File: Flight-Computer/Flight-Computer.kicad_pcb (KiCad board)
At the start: 4 copper layers, 93.7 x 43.7 mm, 120 parts, among them J1 Jumper_NO, J2 Jumper_NO, P1 647676-2, P10 Micro_SD_Card, P2 1546551-2, P3 3220-20-0200-00, P4 440054-3, P5 440054-3, P6 440054-3, P7 440054-3, P8 USB, P9 1984659, Q1 QS5U17TR, Q2 QS5U17TR, Q3 QS5U17TR, Q4 QS5U17TR, Q5 QS5U17TR, Q6 QS5U17TR, U1 STM32H750VBTx, U10 TS391IYLT, U11 TS391IYLT, U12 BMM350, U13 S-85S1AB33-I6T1U, U2 LMS8117AMP-3.3_NOPB, U3 BMI323, U4 MAX-8C-0-10, U5 BMP390, U6 SST25VF040B-50-4I-S2AE-T, U7 RFM95W-868S2, U8 CP2102-GMR(QFN28), U9 TS391IYLT, Y1 ECS-240-18-33-JGN-TR

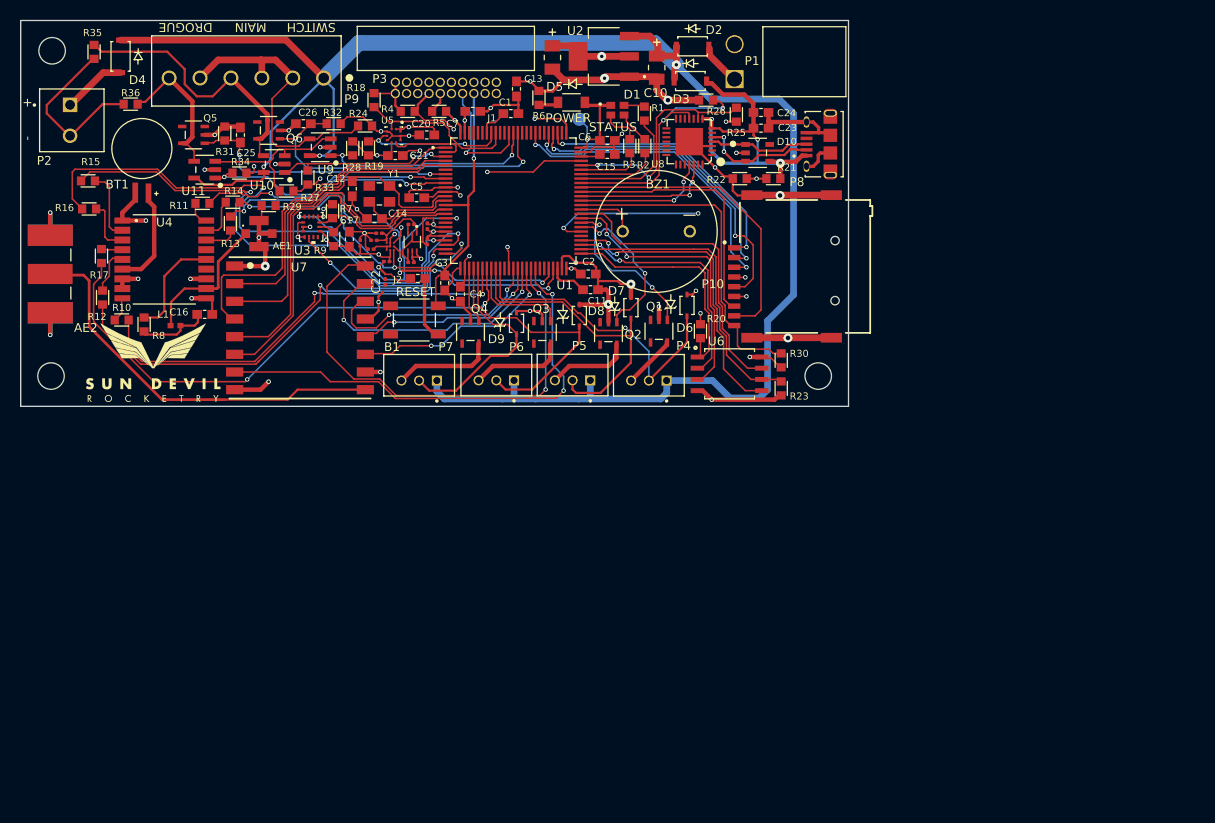
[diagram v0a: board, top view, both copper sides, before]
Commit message: LDO update
Changed buck 1.8V converter to LDO
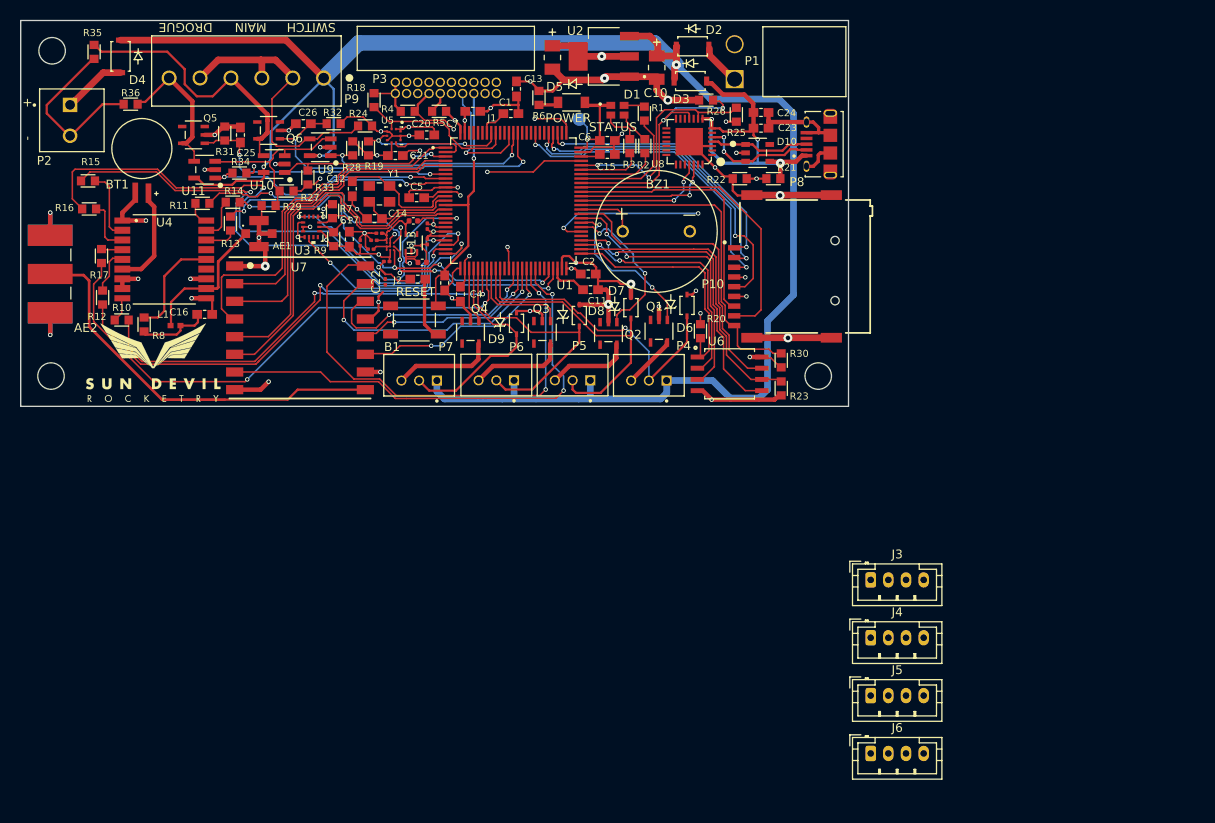
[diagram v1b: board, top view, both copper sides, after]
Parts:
- removed L2: 2.2uH, Inductor_SMD:L_0201_0603Metric
- added C30: 1uF, Capacitor_SMD:C_0402_1005Metric, F.Cu at (137.4, 80.6)
- added J3: Conn_01x04, Connector_JST:JST_PH_B4B-PH-K_1x04_P2.00mm_Vertical, F.Cu at (189.2, 121.2)
- added J4: Conn_01x04, Connector_JST:JST_PH_B4B-PH-K_1x04_P2.00mm_Vertical, F.Cu at (189.2, 127.8)
- added J5: Conn_01x04, Connector_JST:JST_PH_B4B-PH-K_1x04_P2.00mm_Vertical, F.Cu at (189.2, 134.3)
- added J6: Conn_01x04, Connector_JST:JST_PH_B4B-PH-K_1x04_P2.00mm_Vertical, F.Cu at (189.2, 140.9)
- C29: value 10uF -> 1uF; footprint Capacitor_SMD:C_0201_0603Metric -> Capacitor_SMD:C_0402_1005Metric
- U13: value S-85S1AB33-I6T1U -> MIC5365-1.8YC5-TR; footprint S85S1A:SNT-6A-A-PKG_PG006-A-P-SD-2.1_ABL -> MIC5365:SC-70_C5_MCH-L
- moved C29 1.26 mm to (138.4, 85.3), turned to 0 degrees
- moved U13 0.14 mm to (137.2, 83.1), turned to 90 degrees
- moved J2 0.08 mm to (137.9, 87.2)
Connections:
- U13 pad 1: 1.8V -> 3.3V
- U13 pad 3: Net-(U13-SW) -> 3.3V
- U13 pad 4: Earth -> unconnected-(U13-NC-Pad4)
- U13 pad 5: 3.3V -> 1.8V
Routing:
- net Earth: track 245.1 -> 240.6 mm, vias 43 -> 44
- net 3.3V: track 95.7 -> 97.4 mm
- net Net-(U13-SW): track 1.06 -> 0.00 mm
- net 1.8V: track 8.09 -> 7.54 mm

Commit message: SPI Flash Daisy chain
need to review and likely rewire the daisy chain
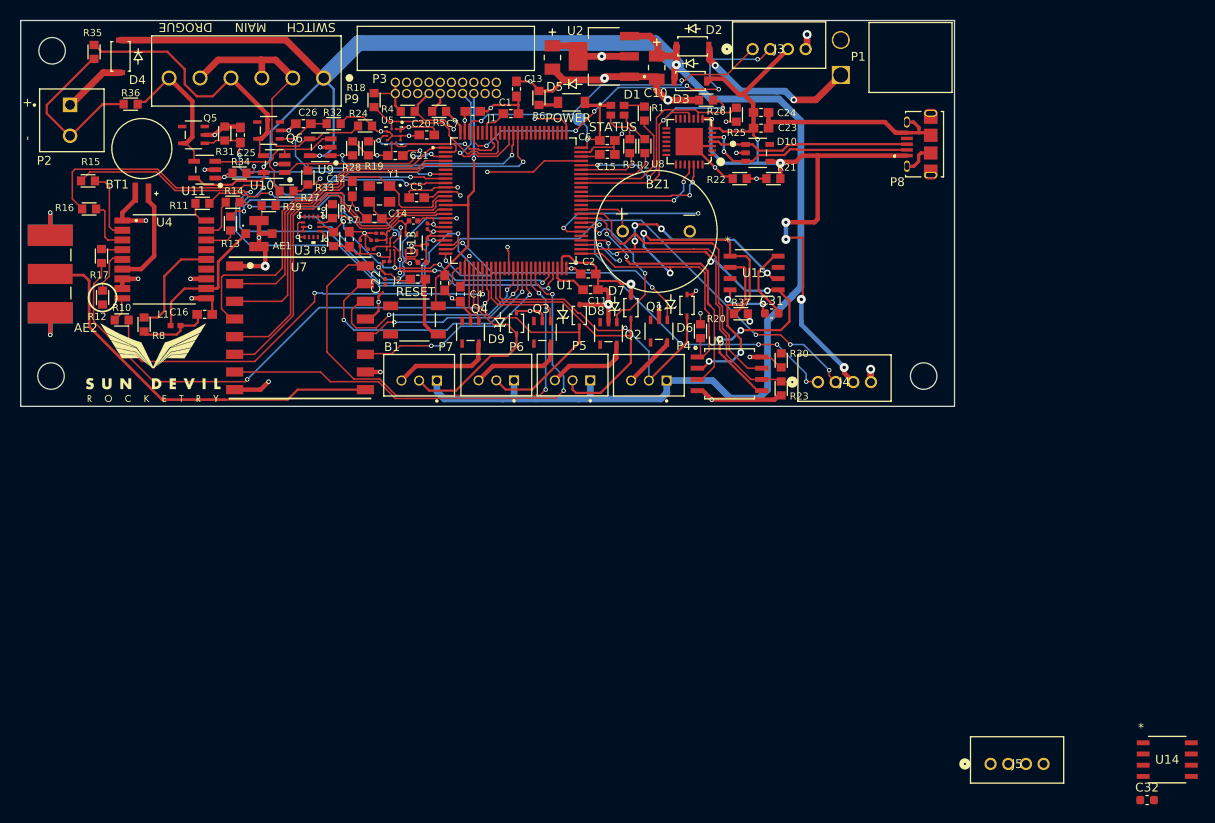
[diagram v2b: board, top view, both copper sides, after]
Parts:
- removed J6: Conn_01x04, Connector_JST:JST_PH_B4B-PH-K_1x04_P2.00mm_Vertical
- removed P10: Micro_SD_Card, Flight-Computer:MEM2075-00-140-01-A
- added C31: 0.1u, Capacitor_SMD:C_0603_1608Metric, F.Cu at (178.0, 91.1)
- added C32: 0.1u, Capacitor_SMD:C_0603_1608Metric, F.Cu at (220.5, 146.2)
- added R37: 10k, Flight-Computer-Mac:RES_0603, F.Cu at (174.5, 91.1)
- added U14: SST25VF512A-33-4I-SAE, SST25:SOIC8_SA_SST_MCH, F.Cu at (222.8, 141.6)
- added U15: SST25VF512A-33-4I-SAE, SST25:SOIC8_SA_SST_MCH, F.Cu at (176.0, 86.5)
- C30: value 10uF -> 1uF
- J3, J4, J5: value Conn_01x04 -> 440054-4; footprint Connector_JST:JST_PH_B4B-PH-K_1x04_P2.00mm_Vertical -> 440054_4:CONN_440054-4_TEC
- moved J3 61.6 mm to (175.8, 61.1)
- moved J4 29.6 mm to (183.2, 98.8)
- moved J5 15.6 mm to (202.8, 142.1)
- moved P1 12.0 mm to (185.8, 64.1)
- moved H3 11.9 mm to (195.2, 98.2)
- moved P8 11.4 mm to (196.0, 71.9)
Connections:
- C30 pad 1: Earth -> 1.8V
- C30 pad 2: 1.8V -> Earth
- J3 pad 1: PUART_TX -> PORT1_TX
- J3 pad 2: PUART_RX -> PORT1_RX
- J4 pad 1: PUART_TX -> PORT2_TX
- J4 pad 2: PUART_RX -> PORT2_RX
- J5 pad 1: PUART_TX -> PORT3_RX
- J5 pad 2: PUART_RX -> PORT3_TX
- U1 pad 24: IMU_INT2 -> PORT2_TX
- U1 pad 25: GPS_INT -> PORT2_RX
- U1 pad 97: unconnected-(U1-PE0-Pad97) -> PORT1_RX
- U1 pad 98: unconnected-(U1-PE1-Pad98) -> PORT1_TX
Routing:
- net PORT2_RX: track 0.00 -> 64.3 mm, vias 0 -> 4
- net GPS_INT: track 56.3 -> 0.05 mm, vias 2 -> 0
- net 5V: track 38.4 -> 91.4 mm, vias 3 -> 7
- net PORT2_TX: track 0.00 -> 49.5 mm, vias 0 -> 4
- net PORT1_RX: track 0.00 -> 42.9 mm, vias 0 -> 6
- net SD_CLK: track 38.3 -> 0.00 mm, vias 2 -> 0
- net ~{SD_DETECT}: track 37.5 -> 0.57 mm
- net PORT1_TX: track 0.00 -> 36.8 mm, vias 0 -> 2
- net SD_CMD: track 35.6 -> 0.00 mm, vias 2 -> 0
- net SD_DAT1: track 35.4 -> 0.03 mm
- net SD_DAT3: track 33.4 -> 0.00 mm, vias 2 -> 0
- net SD_DAT2: track 30.3 -> 0.00 mm, vias 2 -> 0
- net SD_DAT0: track 29.5 -> 0.00 mm
- net ~{FLASH_SS}: track 27.7 -> 55.2 mm, vias 0 -> 2
- net IMU_INT2: track 21.9 -> 0.00 mm, vias 2 -> 0
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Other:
- board size 93.7 x 43.7 mm -> 105.7 x 43.7 mm
